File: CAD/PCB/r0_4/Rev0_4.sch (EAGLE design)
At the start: 45 parts, among them IC1 EEPROM, U1 ARDUINO_SHIELDNOHOLESORLABELS

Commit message: Changed output channel series resistors in CAD files from 1k to 750-ohm (current-limits outputs to a max of 10mA, previously 8.6mA)
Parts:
- R6, R7, R8, R9: value 1k -> 750
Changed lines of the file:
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@@
 <part name="LEDS" library="SparkFun" deviceset="M02" device="PTH"/>
 <part name="RN1" library="resistor-sil" deviceset="GE07R" device=""/>
-<part name="R6" library="SparkFun" deviceset="RESISTOR" device="AXIAL-0.3" value="1k"/>
-<part name="R7" library="SparkFun" deviceset="RESISTOR" device="AXIAL-0.3" value="1k"/>
-<part name="R8" library="SparkFun" deviceset="RESISTOR" device="AXIAL-0.3" value="1k"/>
-<part name="R9" library="SparkFun" deviceset="RESISTOR" device="AXIAL-0.3" value="1k"/>
+<part name="R6" library="SparkFun" deviceset="RESISTOR" device="AXIAL-0.3" value="750"/>
+<part name="R7" library="SparkFun" deviceset="RESISTOR" device="AXIAL-0.3" value="750"/>
+<part name="R8" library="SparkFun" deviceset="RESISTOR" device="AXIAL-0.3" value="750"/>
+<part name="R9" library="SparkFun" deviceset="RESISTOR" device="AXIAL-0.3" value="750"/>
 <part name="MISOMOSI" library="SparkFun" deviceset="M02" device="PTH"/>
 <part name="CLOCK" library="SparkFun" deviceset="M02" device="PTH"/>

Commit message: Replaced bipolar voltage converter in PCB design (and BOM) with a lower power, lower cost, more available part from the same family.
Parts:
- removed U$7: TDK_LAMBDA_5_TO_BIPOLAR12V, JoshParts:TDK_LAMBDA_5_TO_BIPOLAR12V
- added U$8: TDK_LAMBDA_5_TO_BI_12_125MA, JoshParts:TDK_LAMBDA_5_TO_BI_12_125MA
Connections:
- net GND: now also U$8.P$2, U$8.P$3, U$8.P$5; no longer U$7.2, U$7.3, U$7.5
- net N$23: now also U$8.P$4; no longer U$7.4
- net N$28: now also U$8.P$7; no longer U$7.7
- net VCC: now also U$8.P$1; no longer U$7.1
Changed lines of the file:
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@@
 <part name="P+6" library="SparkFun" deviceset="VCC" device=""/>
 <part name="GND5" library="SparkFun" deviceset="GND" device=""/>
-<part name="U$7" library="JoshParts" deviceset="TDK_LAMBDA_5_TO_BIPOLAR12V" device=""/>
+<part name="U$8" library="JoshParts" deviceset="TDK_LAMBDA_5_TO_BI_12_125MA" device=""/>
 </parts>
 <sheets>
@@
 <instance part="P+6" gate="1" x="68.58" y="-2.54"/>
 <instance part="GND5" gate="1" x="83.82" y="-20.32"/>
-<instance part="U$7" gate="G$1" x="83.82" y="-7.62"/>
+<instance part="U$8" gate="G$1" x="81.28" y="-7.62"/>
 </instances>
 <busses>
@@
 <wire x1="71.12" y1="-10.16" x2="71.12" y2="-12.7" width="0.1524" layer="91"/>
 <wire x1="71.12" y1="-12.7" x2="73.66" y2="-12.7" width="0.1524" layer="91"/>
-<pinref part="U$7" gate="G$1" pin="2"/>
-<pinref part="U$7" gate="G$1" pin="3"/>
+<pinref part="U$8" gate="G$1" pin="P$2"/>
+<pinref part="U$8" gate="G$1" pin="P$3"/>
 <junction x="73.66" y="-12.7"/>
-<pinref part="U$7" gate="G$1" pin="5"/>
+<pinref part="U$8" gate="G$1" pin="P$5"/>
+<wire x1="93.98" y1="-10.16" x2="91.44" y2="-10.16" width="0.1524" layer="91"/>
 </segment>
 </net>
@@
 <pinref part="P+6" gate="1" pin="VCC"/>
 <wire x1="73.66" y1="-2.54" x2="68.58" y2="-2.54" width="0.1524" layer="91"/>
-<pinref part="U$7" gate="G$1" pin="1"/>
+<pinref part="U$8" gate="G$1" pin="P$1"/>
+<wire x1="73.66" y1="-2.54" x2="73.66" y2="-5.08" width="0.1524" layer="91"/>
 </segment>
 </net>
@@
 <wire x1="93.98" y1="-12.7" x2="104.14" y2="-12.7" width="0.1524" layer="91"/>
 <wire x1="104.14" y1="-12.7" x2="104.14" y2="5.08" width="0.1524" layer="91"/>
-<pinref part="U$7" gate="G$1" pin="4"/>
+<pinref part="U$8" gate="G$1" pin="P$4"/>
+<wire x1="93.98" y1="-12.7" x2="91.44" y2="-12.7" width="0.1524" layer="91"/>
 </segment>
 </net>
@@
 <wire x1="83.82" y1="5.08" x2="93.98" y2="5.08" width="0.1524" layer="91"/>
 <wire x1="93.98" y1="5.08" x2="93.98" y2="-2.54" width="0.1524" layer="91"/>
-<pinref part="U$7" gate="G$1" pin="7"/>
-</segment>
-</net>
+<wire x1="93.98" y1="-2.54" x2="93.98" y2="-5.08" width="0.1524" layer="91"/>
+<pinref part="U$8" gate="G$1" pin="P$7"/>
+<wire x1="93.98" y1="-5.08" x2="91.44" y2="-5.08" width="0.1524" layer="91"/>
+</segment>
+</net>

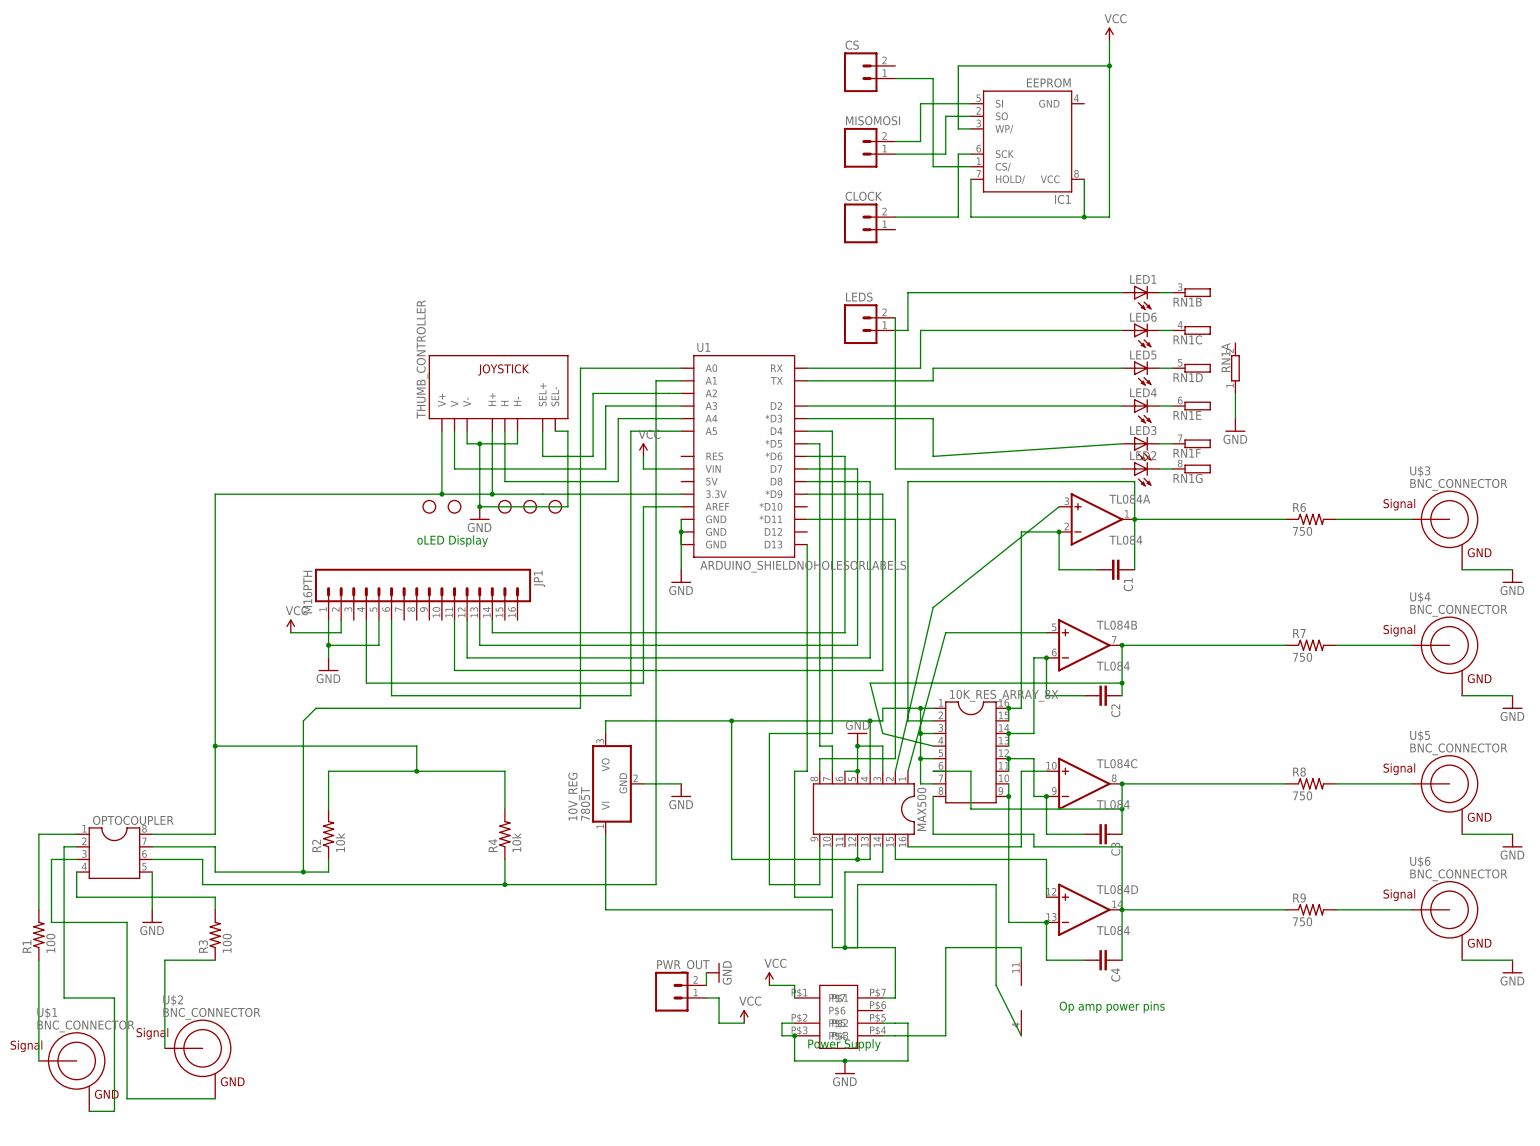
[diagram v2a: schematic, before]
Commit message: -Cleaned up schematic (preliminary - final version will require re-routing the board)
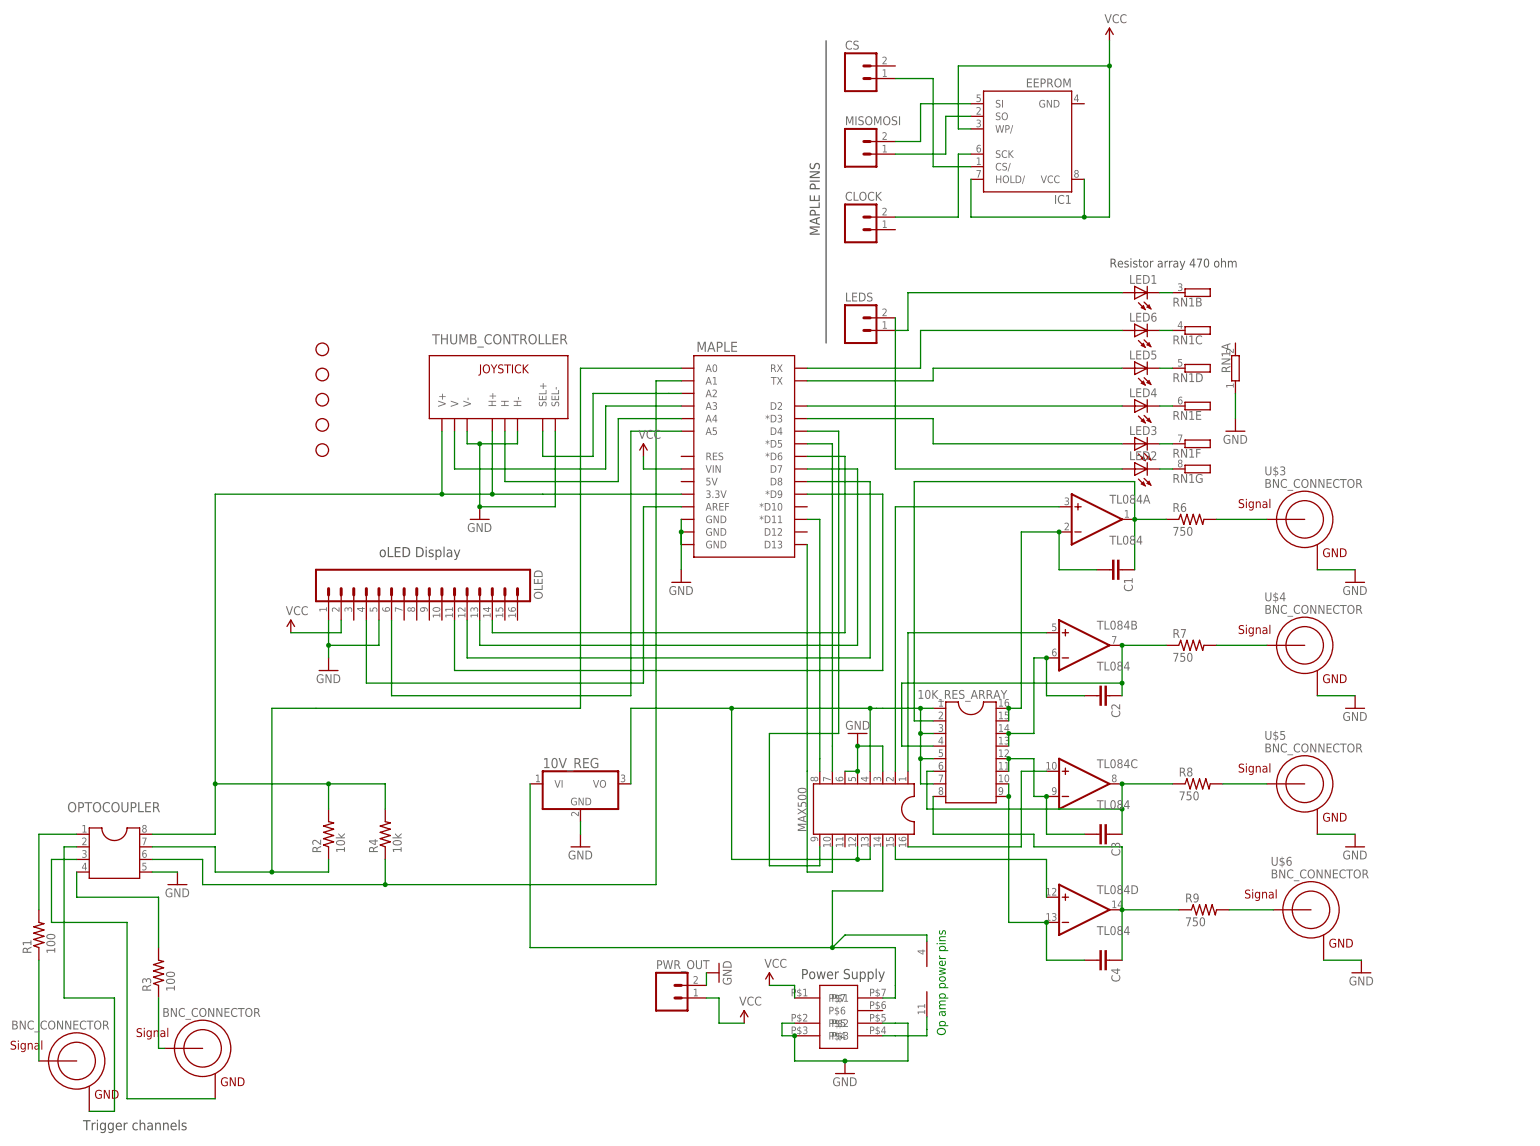
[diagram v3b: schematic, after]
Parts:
- renumbered 10K_RES_ARRAY_8X to 10K_RES_ARRAY, JP1 to OLED, U1 to MAPLE
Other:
- note added: "MAPLE PINS"
- note added: "Resistor array 470 ohm"
- note added: "Trigger channels"
- moved on the sheet: 10V_REG, R3, R4, R6, R7, R8, R9, U$3, U$4, U$5, U$6
